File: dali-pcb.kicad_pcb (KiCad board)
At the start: 2 copper layers, 180.5 x 113 mm, 60 parts, among them J1 12-22.5V DC, J10 5V DC, J11 5V DC, J12 5V DC, J13 5V DC, J14 5V DC, J15 GND, J2 DALI BUS, J20 LOLIN-S3 (L), J21 LOLIN-S3 (R), J22 ESP32-S3-DEVKITC-1 (L), J23 ESP32-S3-DEVKITC-1 (R), J24 LOLIN-S3-MINI (L), J25 LOLIN-S3-MINI (R), J26 LOLIN-S2-MINI (L), J27 LOLIN-S2-MINI (R), J3 DALI BUS, J30 FTDI-MCU, J31 UART-DALI, J4 DALI BUS, J40 A10-0, J41 A5-0, J42 A5-5, J43 A2-0, J44 A2-2, J45 A2-4, J46 A2-6, J47 A2-8, J50 D8-11, J51 D4-11, J52 D4-16, J53 D2-11, J54 D2-13, J55 D2-16, J56 D2-18, J60 D1-11, J61 D1-12, J62 D1-13, J63 D1-14, Q1 PZT2222A, Q2 MMBT2222A, U1 TCLT1000, U2 TCLT1000

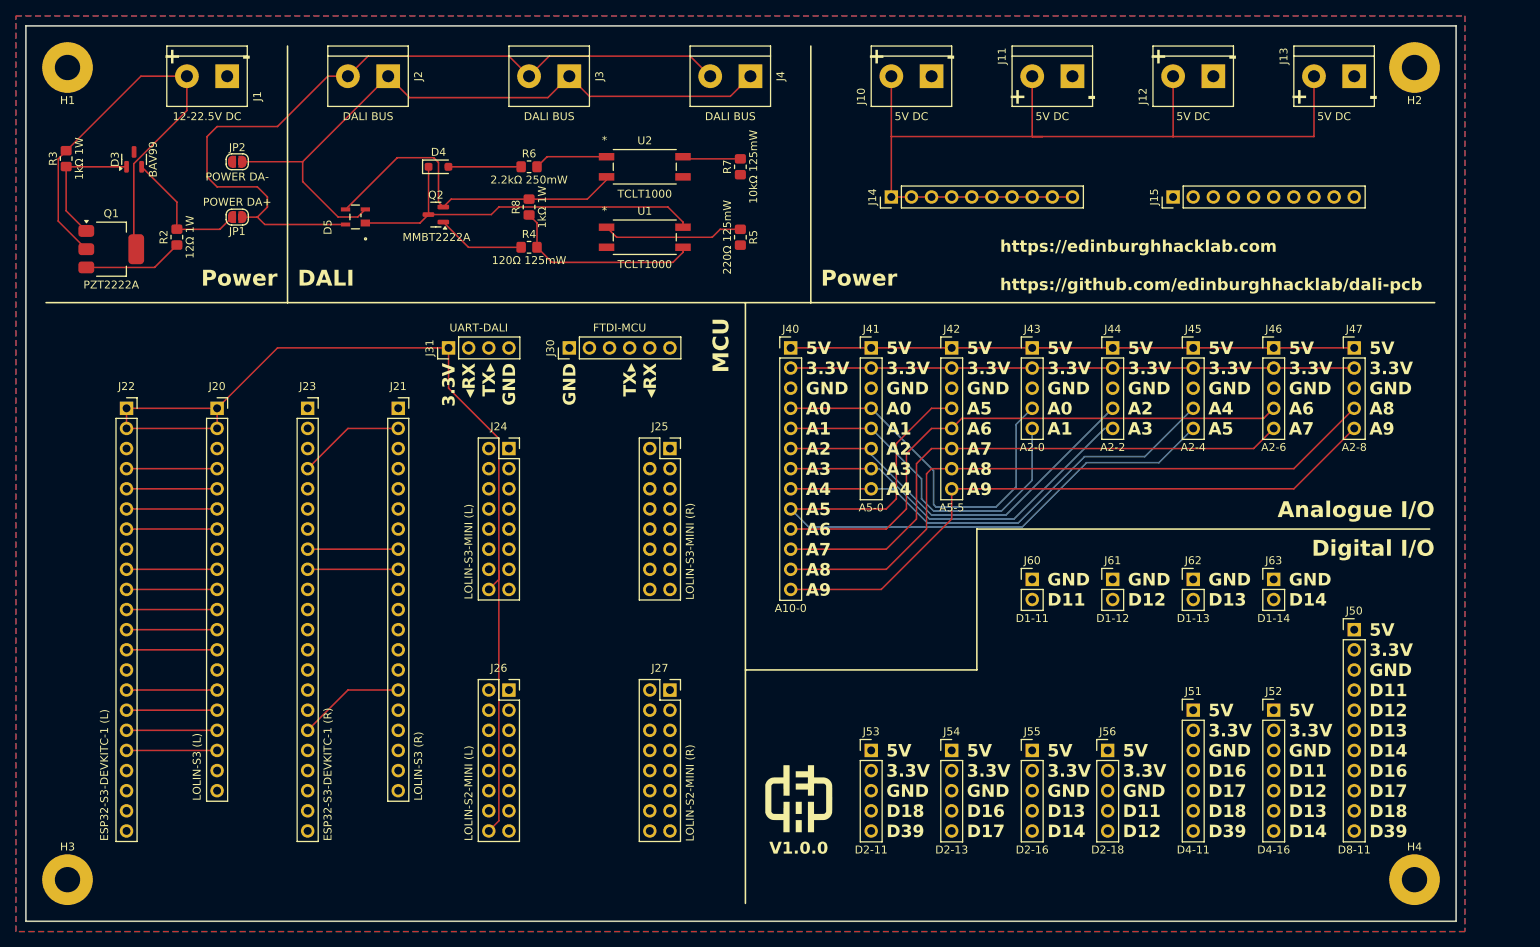
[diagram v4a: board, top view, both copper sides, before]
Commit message: First routing attempt
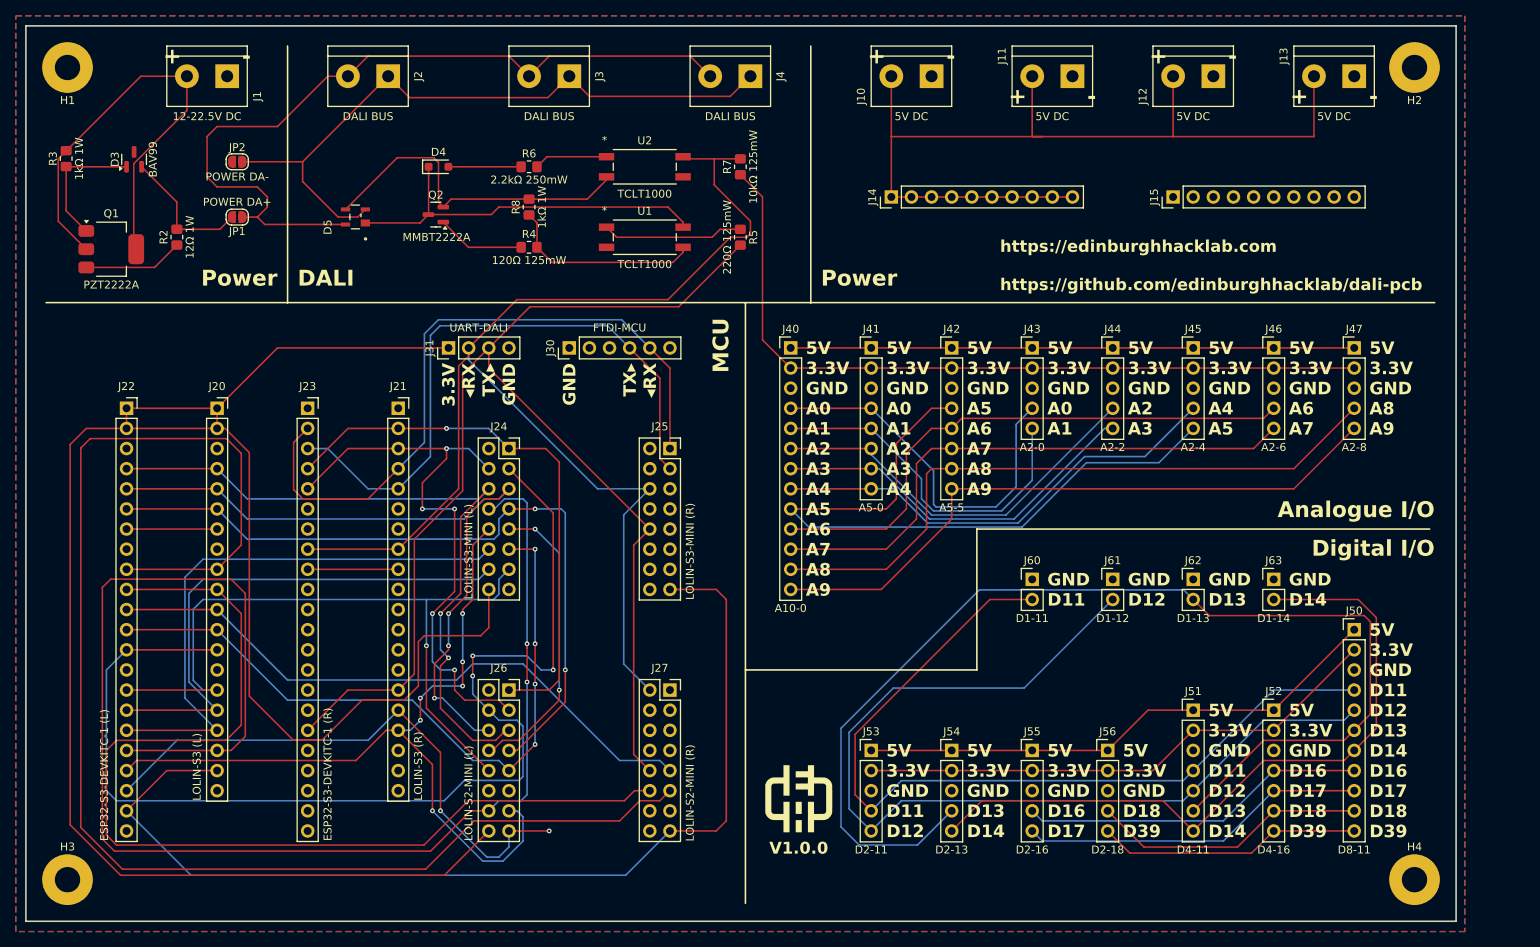
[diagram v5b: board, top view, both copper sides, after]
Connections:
- J25 pad 6: unconnected-(J25-Pin_6-Pad6) -> /DALI/DALI_RX
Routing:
- net /IO/IO_D12: track 11.4 -> 306.4 mm, vias 0 -> 2
- net /IO/IO_D13: track 0.00 -> 245.8 mm, vias 0 -> 6
- net +3.3V: track 198.4 -> 422.0 mm
- net /IO/IO_D16: track 11.4 -> 221.2 mm
- net +5V: track 186.7 -> 385.0 mm
- net /IO/IO_D11: track 11.4 -> 179.4 mm
- net /IO/IO_D17: track 11.4 -> 174.6 mm
- net /IO/IO_D14: track 0.00 -> 162.1 mm, vias 0 -> 2
- net /DALI/DALI_TX: track 13.5 -> 162.0 mm
- net /DALI/DALI_RX: track 18.4 -> 160.0 mm
- net /IO/IO_A2: track 61.6 -> 192.6 mm, vias 0 -> 3
- net /IO/IO_D18: track 11.4 -> 113.6 mm
- net /IO/FTDI_MCU_RXD: track 0.00 -> 86.5 mm
- net /IO/IO_A5: track 98.0 -> 180.0 mm, vias 0 -> 2
- net /IO/IO_A8: track 95.1 -> 175.8 mm, vias 0 -> 1
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
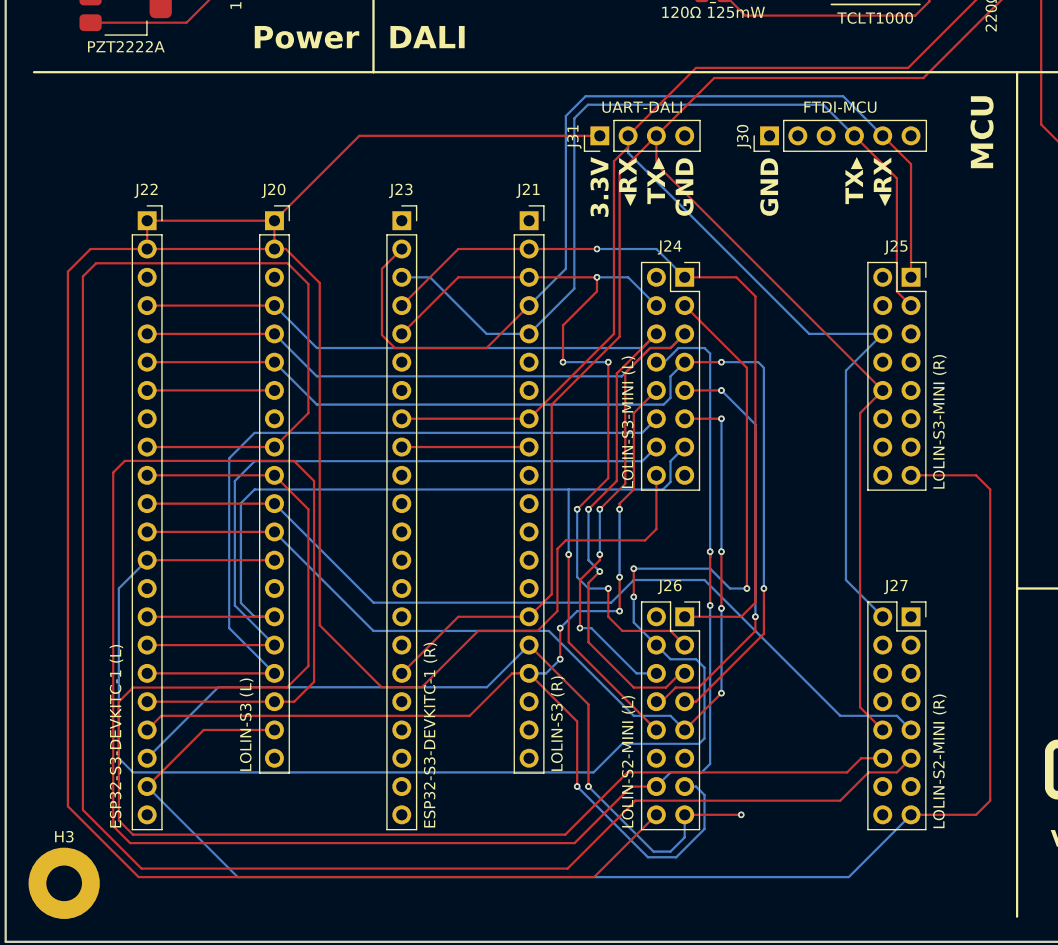
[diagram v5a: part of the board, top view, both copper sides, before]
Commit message: Swap order of microcontrollers to avoid a mess of tracks
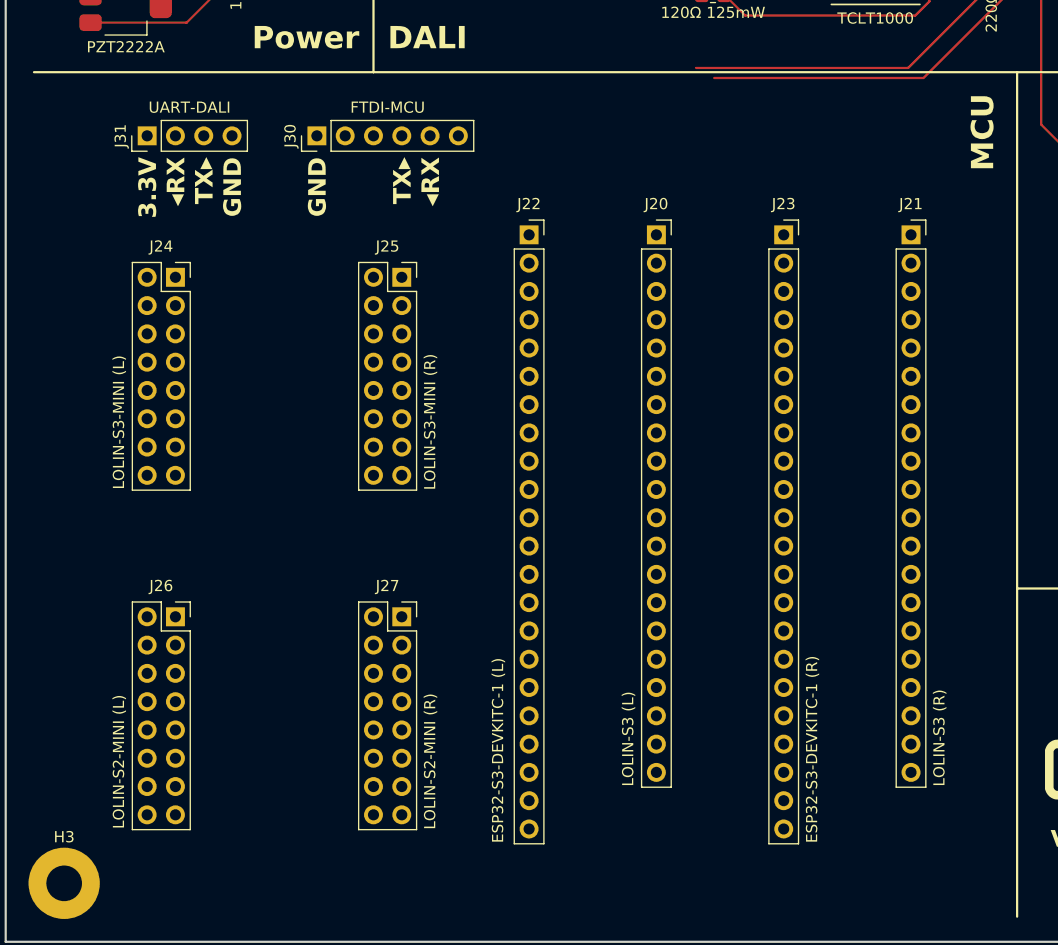
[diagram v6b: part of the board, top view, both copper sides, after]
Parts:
- moved J24 45.7 mm to (30.5, 68.6)
- moved J25 45.7 mm to (50.8, 68.6)
- moved J26 45.7 mm to (30.5, 99.1)
- moved J27 45.7 mm to (50.8, 99.1)
- moved J31 40.6 mm to (27.9, 55.9)
- moved J30 40.6 mm to (43.2, 55.9)
- moved J23 34.3 mm to (85.1, 64.8)
- moved J20 34.3 mm to (73.7, 64.8)
- moved J21 34.3 mm to (96.5, 64.8)
- moved J22 34.3 mm to (62.2, 64.8)
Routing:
- net +3.3V: track 422.0 -> 165.4 mm
- net /IO/IO_D12: track 306.4 -> 121.1 mm, vias 2 -> 0
- net /IO/IO_D16: track 221.2 -> 43.8 mm
- net /IO/IO_A2: track 192.6 -> 50.1 mm, vias 3 -> 0
- net /DALI/DALI_TX: track 162.0 -> 29.8 mm
- net +5V: track 385.0 -> 254.0 mm
- net /IO/IO_D17: track 174.6 -> 43.8 mm
- net /DALI/DALI_RX: track 160.0 -> 51.6 mm
- net /IO/IO_D13: track 245.8 -> 143.9 mm, vias 6 -> 0
- net /IO/IO_A5: track 180.0 -> 86.6 mm, vias 2 -> 0
- net /IO/IO_A8: track 175.8 -> 83.6 mm, vias 1 -> 0
- net /IO/IO_A4: track 149.9 -> 58.6 mm, vias 3 -> 0
- net /IO/IO_A3: track 137.7 -> 48.0 mm, vias 2 -> 0
- net /IO/IO_A7: track 159.6 -> 71.4 mm, vias 4 -> 0
- net /IO/FTDI_MCU_RXD: track 86.5 -> 0.00 mm
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
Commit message: Second routing attempt
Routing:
- net /IO/IO_D18: track 34.9 -> 198.9 mm
- net /DALI/DALI_TX: track 29.8 -> 185.0 mm
- net /DALI/DALI_RX: track 51.6 -> 187.5 mm, vias 0 -> 1
- net /IO/IO_D39: track 33.4 -> 154.4 mm
- net +3.3V: track 165.4 -> 260.6 mm
- net /IO/IO_A2: track 50.1 -> 117.0 mm, vias 0 -> 2
- net /IO/IO_D12: track 121.1 -> 184.5 mm
- net /IO/IO_D11: track 107.2 -> 170.5 mm
- net /IO/IO_A8: track 83.6 -> 140.0 mm
- net /IO/IO_A9: track 81.8 -> 138.1 mm
- net /IO/FTDI_MCU_TXD: track 0.00 -> 54.5 mm
- net /IO/IO_A7: track 71.4 -> 125.6 mm
- net /IO/IO_A3: track 48.0 -> 101.2 mm
- net /IO/IO_A5: track 86.6 -> 139.8 mm
- net /IO/IO_A4: track 58.6 -> 111.8 mm
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
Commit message: Everything is now connected
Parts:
- moved J25 29.3 mm to (48.3, 97.8), turned to -90 degrees
- moved J24 19.9 mm to (48.3, 77.5), turned to -90 degrees
- moved J26 19.9 mm to (48.3, 90.2), turned to -90 degrees
- moved J27 11.7 mm to (48.3, 110.5), turned to -90 degrees
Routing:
- net +5V: track 254.0 -> 478.4 mm, vias 0 -> 2
- net /IO/IO_D14: track 90.0 -> 306.6 mm, vias 0 -> 5
- net /IO/IO_D13: track 143.9 -> 339.9 mm, vias 0 -> 3
- net /IO/IO_D17: track 55.2 -> 229.7 mm, vias 0 -> 1
- net /IO/IO_D16: track 55.2 -> 215.3 mm, vias 0 -> 2
- net /DALI/DALI_TX: track 185.0 -> 328.7 mm, vias 0 -> 4
- net /IO/IO_D11: track 170.5 -> 271.7 mm, vias 0 -> 3
- net /IO/IO_D12: track 184.5 -> 271.0 mm, vias 0 -> 1
- net +3.3V: track 260.6 -> 346.7 mm
- net /IO/IO_A8: track 140.0 -> 205.8 mm
- net /IO/IO_A1: track 74.8 -> 137.8 mm, vias 0 -> 3
- net /DALI/DALI_RX: track 187.5 -> 246.3 mm, vias 1 -> 2
- net /IO/IO_A9: track 138.1 -> 195.2 mm
- net /IO/FTDI_MCU_TXD: track 54.5 -> 111.1 mm, vias 0 -> 2
- net /IO/IO_D39: track 154.4 -> 211.0 mm
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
